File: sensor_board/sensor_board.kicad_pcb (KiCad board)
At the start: 2 copper layers, 7.5 x 15 mm, 7 parts, among them J1 Conn_01x03, Q1 Q_Photo_NPN_EBC

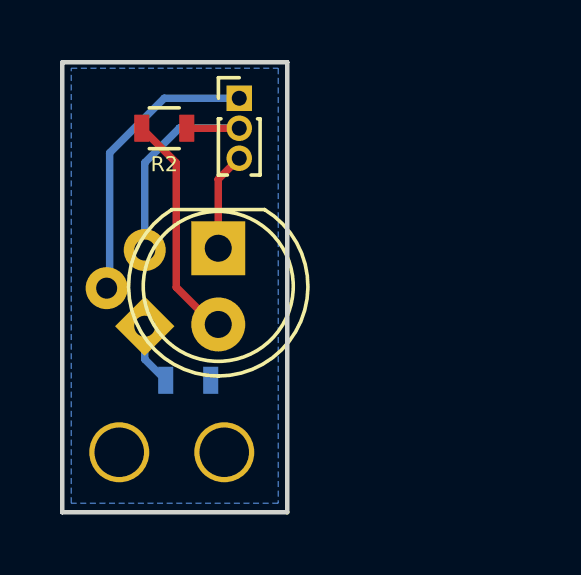
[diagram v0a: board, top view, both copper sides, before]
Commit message: Add more board to seperate sensors
 - not sure where mounting holes are?
 - added gerber
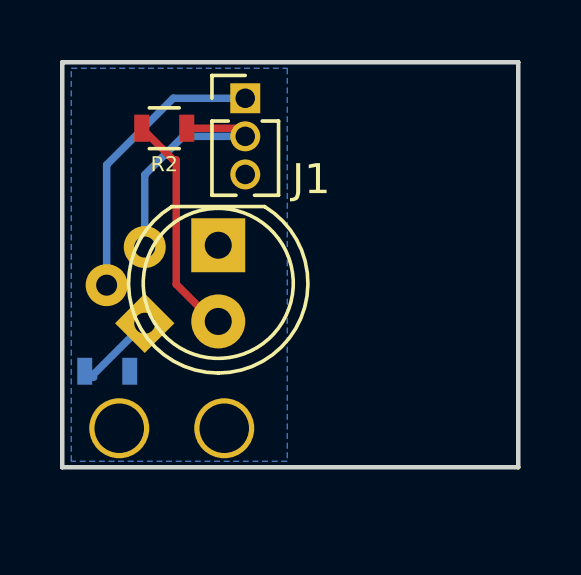
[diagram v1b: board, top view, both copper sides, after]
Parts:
- J1: footprint Pin_Headers:Pin_Header_Straight_1x03_Pitch1.00mm -> Pin_Headers:Pin_Header_Straight_1x03_Pitch1.27mm
- moved R1 2.72 mm to (101.5, 110.3)
- moved REF** 0.80 mm to (102.0, 112.2)
- moved REF** 0.80 mm to (105.5, 112.2)
- moved J1 0.20 mm to (106.1, 101.2)
- moved D1 0.10 mm to (105.2, 106.1)
- moved Q1 0.10 mm to (102.8, 108.7)
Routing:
- net GND: track 3.39 -> 0.00 mm
- net /5v_enable: track 10.8 -> 8.24 mm
- net Net-(Q1-Pad1): track 2.09 -> 2.70 mm
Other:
- board size 7.5 x 15 mm -> 15.2 x 13.5 mm
- net class Default: clearance 0.1 -> 0.16
- rule trace_clearance: 0.1 -> 0.16
